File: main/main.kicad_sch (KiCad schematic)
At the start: 5 parts, among them SW1 SW_DPST_x2

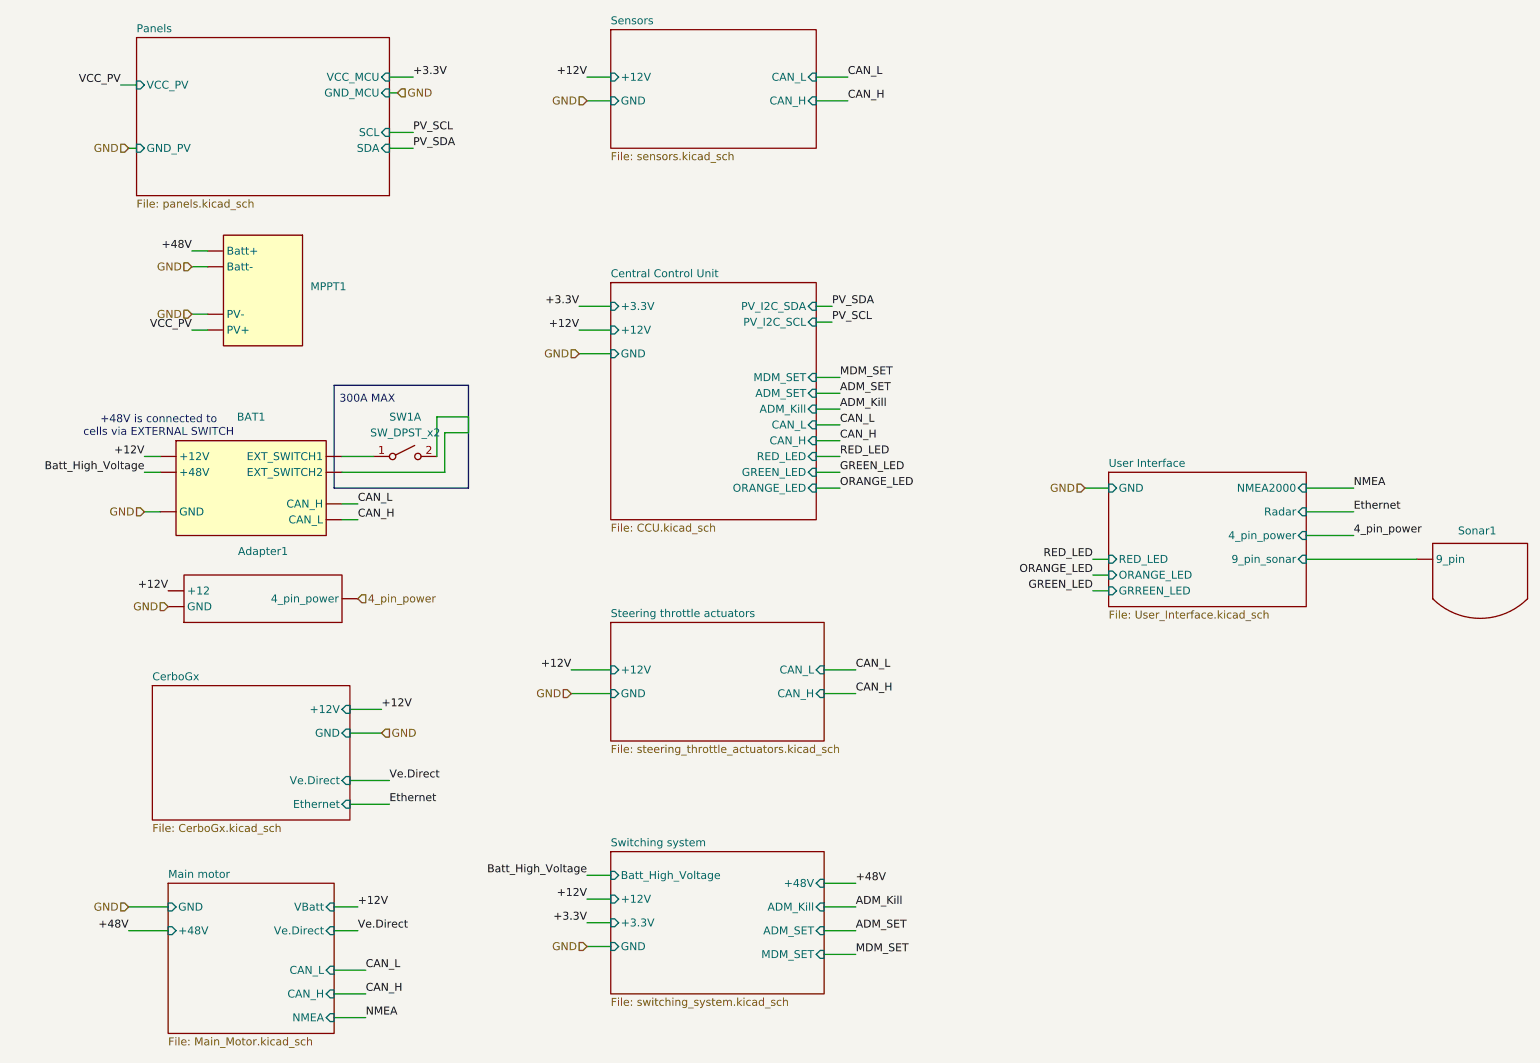
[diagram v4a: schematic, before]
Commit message: Updated digital gateway position. Removed NMEA lines
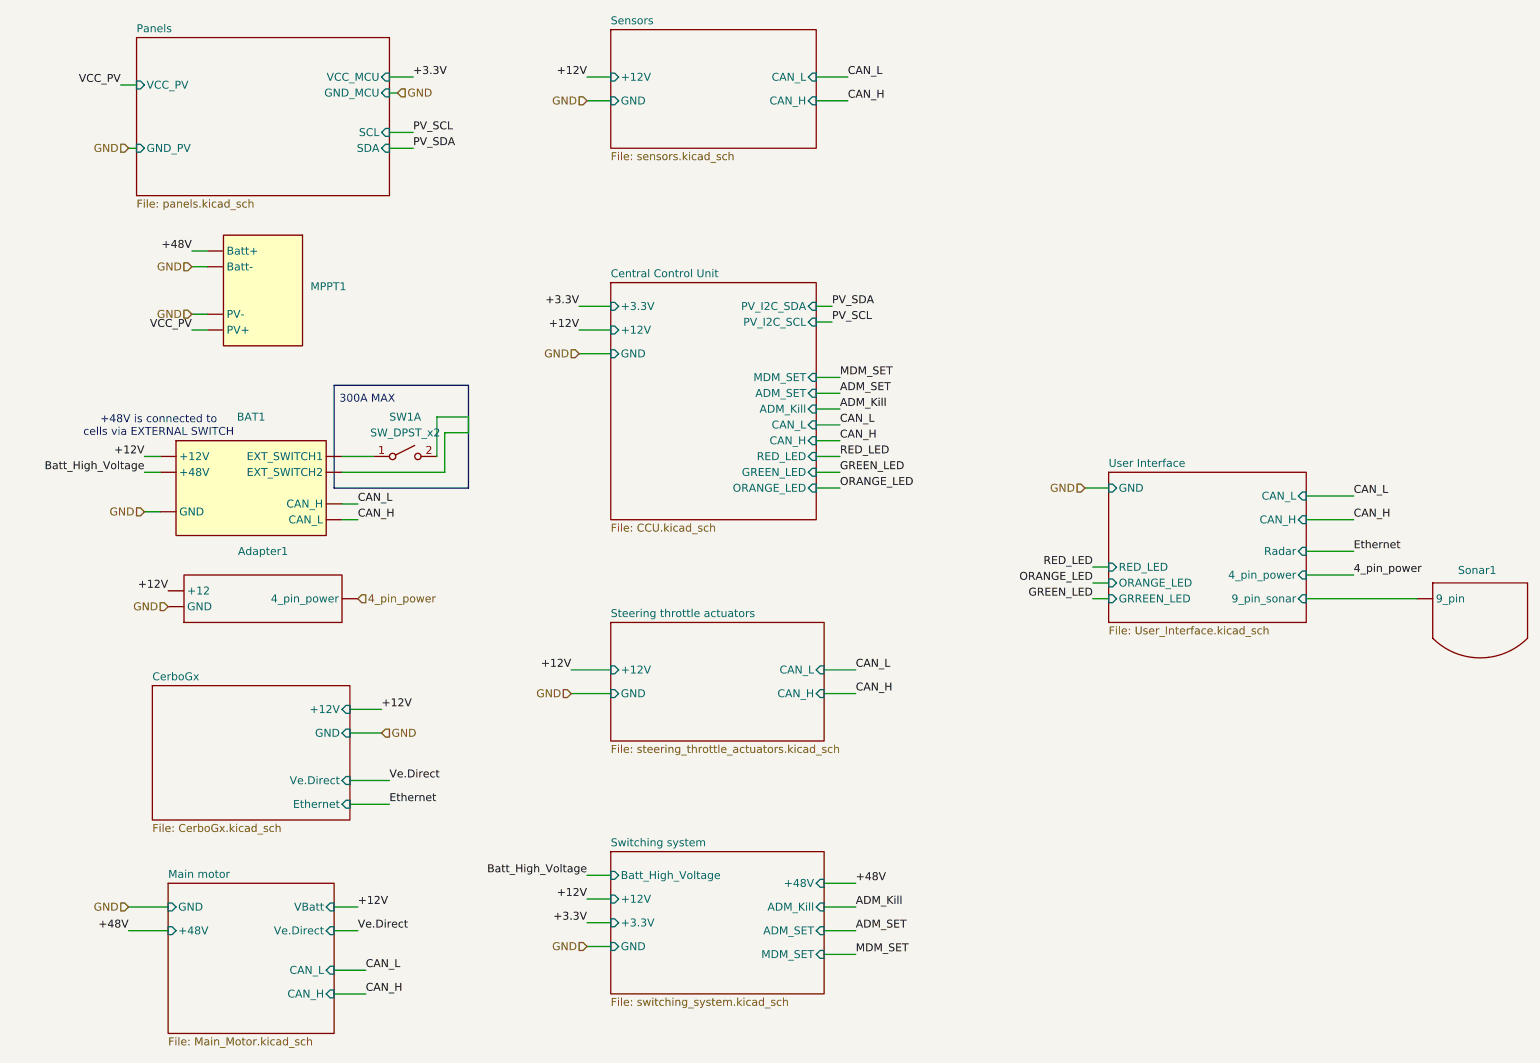
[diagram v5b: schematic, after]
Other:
- sheet Main motor ports: added none; removed NMEA
- sheet User Interface ports: added CAN_H, CAN_L; removed NMEA2000
- moved on the sheet: Sonar1
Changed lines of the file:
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@@
 	(wire
 		(pts
-			(xy 231.14 96.52) (xy 238.76 96.52)
-		)
-		(stroke
-			(width 0)
-			(type default)
-		)
-	)
-	(wire
-		(pts
 			(xy 152.4 83.82) (xy 156.21 83.82)
 		)
@@
 	(wire
 		(pts
-			(xy 238.76 104.14) (xy 231.14 104.14)
+			(xy 238.76 110.49) (xy 231.14 110.49)
 		)
 		(stroke
@@
 	(wire
 		(pts
-			(xy 196.85 110.49) (xy 199.39 110.49)
+			(xy 196.85 111.76) (xy 199.39 111.76)
 		)
 		(stroke
@@
 	(wire
 		(pts
-			(xy 231.14 100.33) (xy 238.76 100.33)
+			(xy 231.14 106.68) (xy 238.76 106.68)
 		)
 		(stroke
@@
 	(wire
 		(pts
-			(xy 231.14 107.95) (xy 248.92 107.95)
+			(xy 231.14 114.3) (xy 248.92 114.3)
 		)
 		(stroke
@@
 	(wire
 		(pts
+			(xy 231.14 97.79) (xy 238.76 97.79)
+		)
+		(stroke
+			(width 0)
+			(type default)
+		)
+	)
+	(wire
+		(pts
 			(xy 74.93 173.99) (xy 80.01 173.99)
 		)
@@
 	(wire
 		(pts
-			(xy 196.85 113.03) (xy 199.39 113.03)
+			(xy 196.85 114.3) (xy 199.39 114.3)
 		)
 		(stroke
@@
 	(wire
 		(pts
-			(xy 92.71 87.63) (xy 96.52 87.63)
+			(xy 231.14 101.6) (xy 238.76 101.6)
 		)
 		(stroke
@@
 	(wire
 		(pts
-			(xy 113.03 129.54) (xy 119.38 129.54)
+			(xy 92.71 87.63) (xy 96.52 87.63)
 		)
 		(stroke
@@
 	(wire
 		(pts
-			(xy 74.93 181.61) (xy 80.01 181.61)
+			(xy 113.03 129.54) (xy 119.38 129.54)
 		)
 		(stroke
@@
 	(wire
 		(pts
-			(xy 196.85 107.95) (xy 199.39 107.95)
+			(xy 196.85 109.22) (xy 199.39 109.22)
 		)
 		(stroke
@@
 		)
 	)
-	(label "NMEA"
-		(at 80.01 181.61 0)
+	(label "CAN_L"
+		(at 238.76 97.79 0)
 		(fields_autoplaced yes)
 		(effects
@@
 		)
 	)
+	(label "CAN_H"
+		(at 238.76 101.6 0)
+		(fields_autoplaced yes)
+		(effects
+			(font
+				(size 1.27 1.27)
+			)
+			(justify left bottom)
+		)
+	)
 	(label "RED_LED"
-		(at 196.85 107.95 180)
+		(at 196.85 109.22 180)
 		(fields_autoplaced yes)
 		(effects
@@
 	)
 	(label "GREEN_LED"
-		(at 196.85 113.03 180)
+		(at 196.85 114.3 180)
 		(fields_autoplaced yes)
 		(effects
@@
 	)
 	(label "Ethernet"
-		(at 238.76 100.33 0)
+		(at 238.76 106.68 0)
 		(fields_autoplaced yes)
 		(effects
@@
 	)
 	(label "4_pin_power"
-		(at 238.76 104.14 0)
+		(at 238.76 110.49 0)
 		(fields_autoplaced yes)
 		(effects
@@
 		)
 	)
-	(label "NMEA"
-		(at 238.76 96.52 0)
-		(fields_autoplaced yes)
-		(effects
-			(font
-				(size 1.27 1.27)
-			)
-			(justify left bottom)
-		)
-	)
 	(label "Ethernet"
 		(at 83.82 147.32 0)
@@
 	)
 	(label "ORANGE_LED"
-		(at 196.85 110.49 180)
+		(at 196.85 111.76 180)
 		(fields_autoplaced yes)
 		(effects
@@
 	(symbol
 		(lib_id "New_Library_0:Sonar")
-		(at 259.08 110.49 0)
+		(at 259.08 116.84 0)
 		(unit 1)
 		(exclude_from_sim no)
@@
 		(dnp no)
 		(property "Reference" "Sonar1"
-			(at 255.524 103.378 0)
+			(at 255.524 109.728 0)
 			(effects
 				(font
@@
 		)
 		(property "Value" "~"
-			(at 267.97 112.7031 0)
+			(at 267.97 119.0531 0)
 			(effects
 				(font
@@
 		)
 		(property "Footprint" ""
-			(at 259.08 110.49 0)
+			(at 259.08 116.84 0)
 			(effects
 				(font
@@
 		)
 		(property "Datasheet" ""
-			(at 259.08 110.49 0)
+			(at 259.08 116.84 0)
 			(effects
 				(font
@@
 		)
 		(property "Description" ""
-			(at 259.08 110.49 0)
+			(at 259.08 116.84 0)
 			(effects
 				(font
@@
 			)
 		)
-		(pin "NMEA" input
-			(at 74.93 181.61 0)
-			(effects
-				(font
-					(size 1.27 1.27)
-				)
-				(justify right)
-			)
-		)
 		(instances
 			(project "main"
@@
 	(sheet
 		(at 199.39 93.98)
-		(size 31.75 21.59)
+		(size 31.75 24.13)
 		(fields_autoplaced yes)
 		(stroke
@@
 		)
 		(property "Sheetfile" "User_Interface.kicad_sch"
-			(at 199.39 116.1546 0)
+			(at 199.39 118.6946 0)
 			(effects
 				(font
@@
 			)
 		)
-		(pin "NMEA2000" input
-			(at 231.14 96.52 0)
-			(effects
-				(font
-					(size 1.27 1.27)
-				)
-				(justify right)
-			)
-		)
 		(pin "4_pin_power" input
-			(at 231.14 104.14 0)
+			(at 231.14 110.49 0)
 			(effects
 				(font
@@
 		)
 		(pin "9_pin_sonar" input
-			(at 231.14 107.95 0)
+			(at 231.14 114.3 0)
 			(effects
 				(font
@@
 		)
 		(pin "RED_LED" input
-			(at 199.39 107.95 180)
+			(at 199.39 109.22 180)
 			(effects
 				(font
@@
 		)
 		(pin "ORANGE_LED" input
-			(at 199.39 110.49 180)
+			(at 199.39 111.76 180)
 			(effects
 				(font
@@
 		)
 		(pin "GRREEN_LED" input
-			(at 199.39 113.03 180)
+			(at 199.39 114.3 180)
 			(effects
 				(font
@@
 		)
 		(pin "Radar" input
-			(at 231.14 100.33 0)
+			(at 231.14 106.68 0)
+			(effects
+				(font
+					(size 1.27 1.27)
+				)
+				(justify right)
+			)
+		)
+		(pin "CAN_L" input
+			(at 231.14 97.79 0)
+			(effects
+				(font
+					(size 1.27 1.27)
+				)
+				(justify right)
+			)
+		)
+		(pin "CAN_H" input
+			(at 231.14 101.6 0)
 			(effects
 				(font
